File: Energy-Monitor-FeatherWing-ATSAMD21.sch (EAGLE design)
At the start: 32 parts

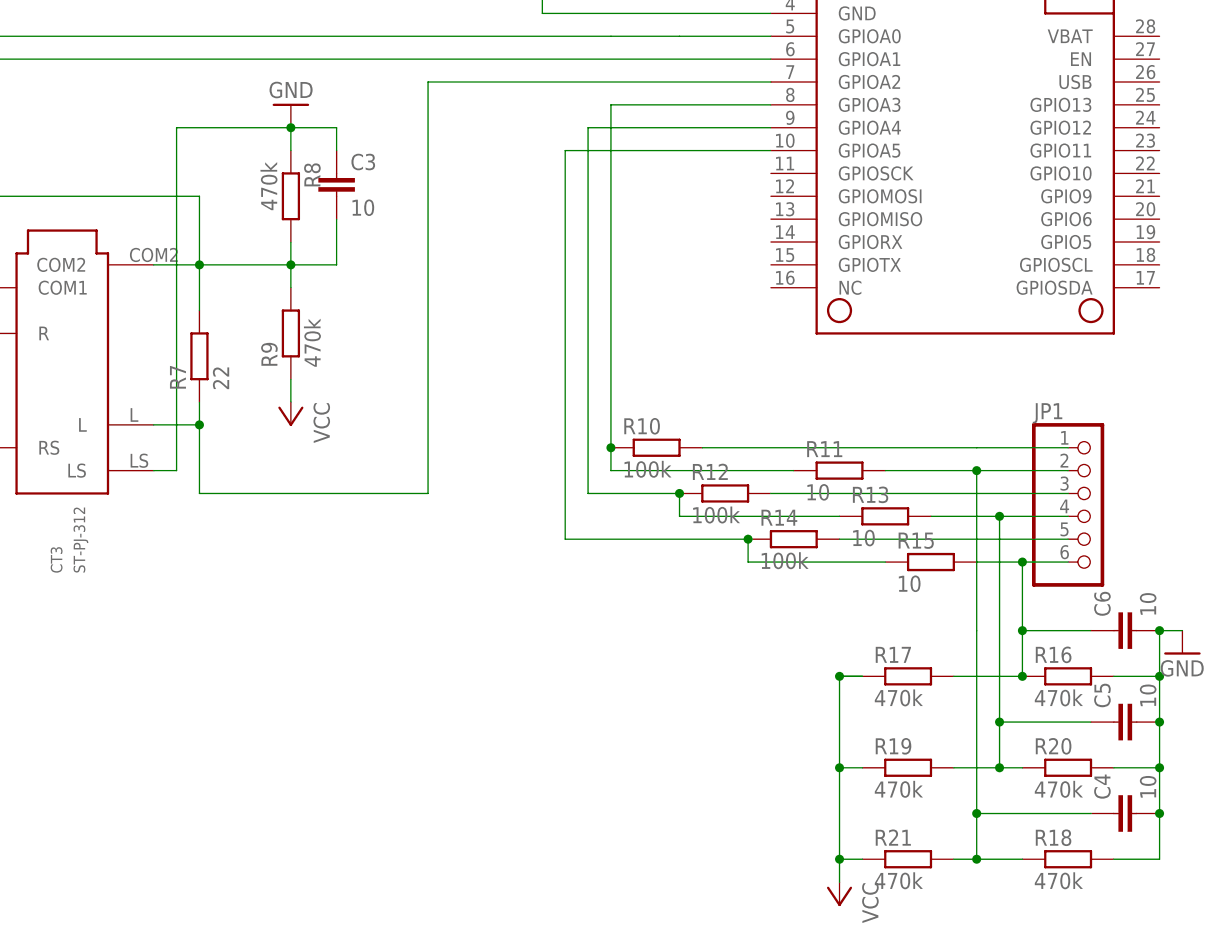
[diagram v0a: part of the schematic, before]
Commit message: Clean up layout and component names
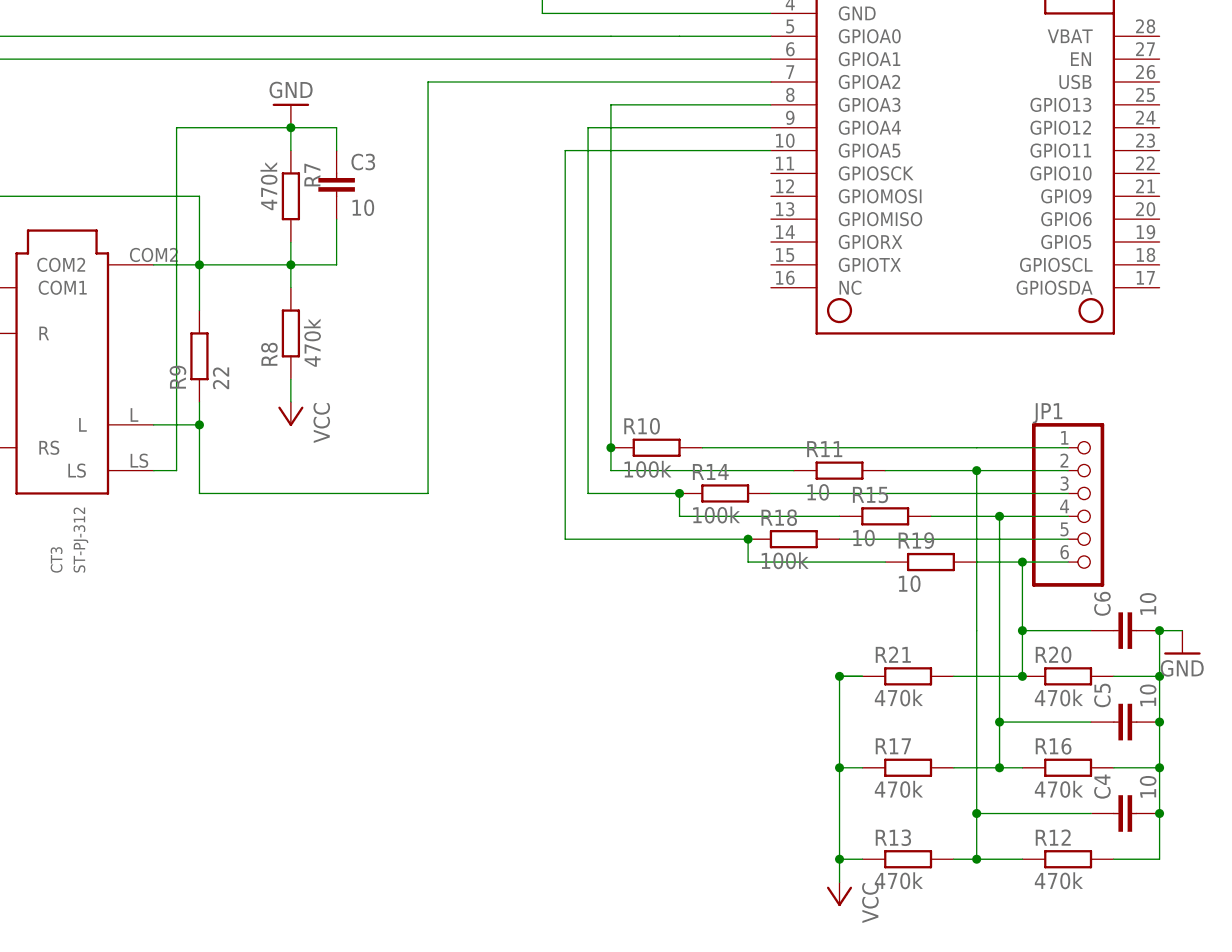
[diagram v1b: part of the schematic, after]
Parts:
- R12: value 100k -> 470k
- R13: value 10 -> 470k
- R18: value 470k -> 100k
- R19: value 470k -> 10
- R7: value 22 -> 470k
- R9: value 470k -> 22
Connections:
- net GND: now also R12.2, R7.1; no longer R18.2, R8.1
- net N$10: now also R18.2; no longer R14.2
- net N$11: now also R18.1, R19.1; no longer R14.1, R15.1
- net N$13: now also R15.2, R16.1, R17.2; no longer R13.2, R19.2, R20.1
- net N$3: now also R9.1; no longer R7.1
- net N$6: now also R19.2, R20.1, R21.2; no longer R15.2, R16.1, R17.2
- net N$7: now also R14.2; no longer R12.2
- net N$8: now also R14.1, R15.1; no longer R12.1, R13.1
- net N$9: now also R12.1, R13.2; no longer R18.1, R21.2
- net VCC: now also R13.1, R8.1; no longer R19.1, R9.1
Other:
- moved on the sheet: R12, R13, R14, R15, R16, R17, R18, R19, R20, R21, R7, R8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

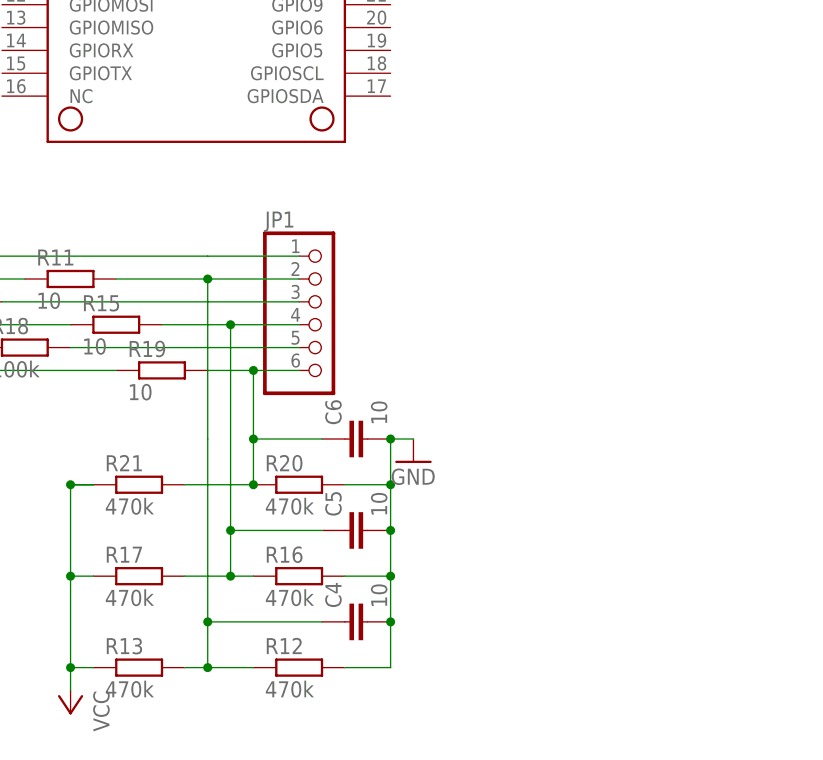
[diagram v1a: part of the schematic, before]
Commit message: Initial work on adding 3-phase bridge rectifier
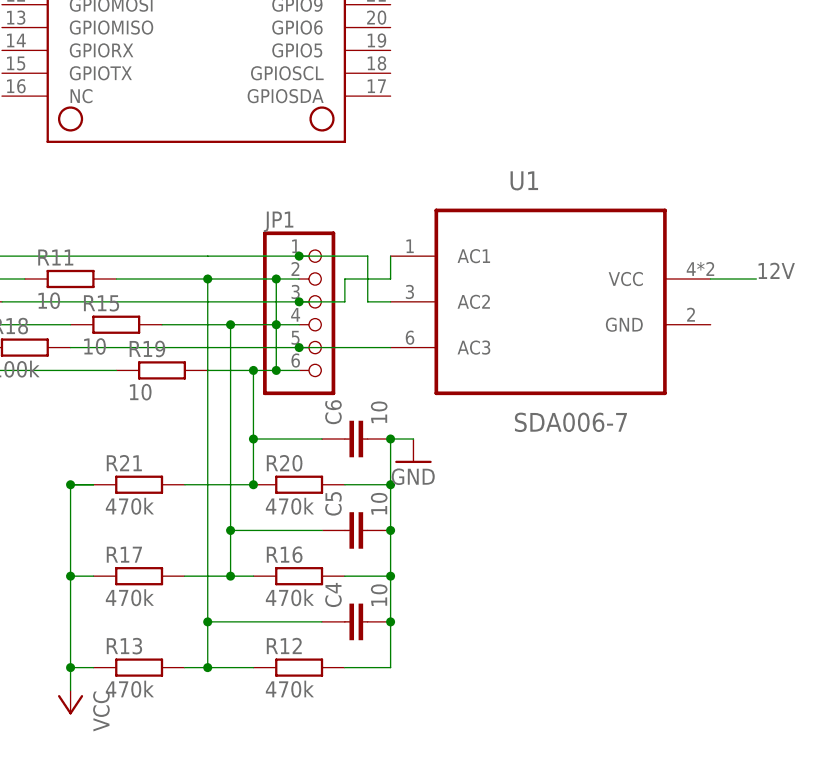
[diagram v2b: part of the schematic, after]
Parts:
- added U1: SDA006-7, Diodes_Inc_By_element14_Batch_1:SDA006-7
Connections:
- removed net N$13: C5.1, JP1.4, R15.2, R16.1, R17.2
- removed net N$6: C6.1, JP1.6, R19.2, R20.1, R21.2
- removed net N$9: C4.1, JP1.2, R11.2, R12.1, R13.2
- new net 12V: U1.VCC
- new net AC_GND: C4.1, C5.1, C6.1, JP1.2, JP1.4, JP1.6, R11.2, R12.1, R13.2, R15.2, R16.1, R17.2, R19.2, R20.1, R21.2
- net N$10: now also U1.AC3
- net N$4: now also U1.AC2
- net N$7: now also U1.AC1
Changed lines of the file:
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@@
 <?xml version="1.0" encoding="utf-8"?>
 <!DOCTYPE eagle SYSTEM "eagle.dtd">
-<eagle version="7.5.0">
+<eagle version="7.6.0">
 <drawing>
 <settings>
@@
 <part name="R16" library="resistor" deviceset="R-EU_" device="R0402" value="470k"/>
 <part name="R13" library="resistor" deviceset="R-EU_" device="R0402" value="470k"/>
+<part name="U1" library="Diodes_Inc_By_element14_Batch_1" deviceset="SDA006-7" device=""/>
 </parts>
 <sheets>
@@
 <instance part="R16" gate="G$1" x="190.5" y="-35.56"/>
 <instance part="R13" gate="G$1" x="172.72" y="-45.72"/>
+<instance part="U1" gate="G$1" x="218.44" y="-2.54"/>
 </instances>
 <busses>
@@
 <pinref part="R10" gate="G$1" pin="2"/>
 <wire x1="180.34" y1="0" x2="149.86" y2="0" width="0.1524" layer="91"/>
+<wire x1="190.5" y1="0" x2="198.12" y2="0" width="0.1524" layer="91"/>
+<wire x1="198.12" y1="0" x2="198.12" y2="-5.08" width="0.1524" layer="91"/>
+<junction x="190.5" y="0"/>
+<pinref part="U1" gate="G$1" pin="AC2"/>
+<wire x1="198.12" y1="-5.08" x2="200.66" y2="-5.08" width="0.1524" layer="91"/>
 </segment>
 </net>
@@
 <pinref part="R14" gate="G$1" pin="2"/>
 <wire x1="190.5" y1="-5.08" x2="157.48" y2="-5.08" width="0.1524" layer="91"/>
+<wire x1="190.5" y1="-5.08" x2="195.58" y2="-5.08" width="0.1524" layer="91"/>
+<junction x="190.5" y="-5.08"/>
+<wire x1="195.58" y1="-5.08" x2="195.58" y2="-2.54" width="0.1524" layer="91"/>
+<wire x1="195.58" y1="-2.54" x2="200.66" y2="-2.54" width="0.1524" layer="91"/>
+<pinref part="U1" gate="G$1" pin="AC1"/>
+<wire x1="200.66" y1="-2.54" x2="200.66" y2="0" width="0.1524" layer="91"/>
 </segment>
 </net>
@@
 </segment>
 </net>
-<net name="N$9" class="0">
+<net name="AC_GND" class="0">
 <segment>
 <pinref part="C4" gate="G$1" pin="1"/>
 <wire x1="193.04" y1="-40.64" x2="180.34" y2="-40.64" width="0.1524" layer="91"/>
-<wire x1="180.34" y1="-40.64" x2="180.34" y2="-20.32" width="0.1524" layer="91"/>
+<wire x1="180.34" y1="-40.64" x2="180.34" y2="-12.7" width="0.1524" layer="91"/>
 <pinref part="R11" gate="G$1" pin="2"/>
 <pinref part="JP1" gate="A" pin="2"/>
 <wire x1="170.18" y1="-2.54" x2="180.34" y2="-2.54" width="0.1524" layer="91"/>
-<wire x1="180.34" y1="-2.54" x2="190.5" y2="-2.54" width="0.1524" layer="91"/>
-<wire x1="180.34" y1="-20.32" x2="180.34" y2="-2.54" width="0.1524" layer="91"/>
+<wire x1="180.34" y1="-2.54" x2="187.96" y2="-2.54" width="0.1524" layer="91"/>
 <junction x="180.34" y="-2.54"/>
 <pinref part="R13" gate="G$1" pin="2"/>
 <pinref part="R12" gate="G$1" pin="1"/>
+<wire x1="187.96" y1="-2.54" x2="190.5" y2="-2.54" width="0.1524" layer="91"/>
+<wire x1="180.34" y1="-12.7" x2="180.34" y2="-2.54" width="0.1524" layer="91"/>
 <wire x1="185.42" y1="-45.72" x2="180.34" y2="-45.72" width="0.1524" layer="91"/>
 <wire x1="180.34" y1="-45.72" x2="177.8" y2="-45.72" width="0.1524" layer="91"/>
@@
 <junction x="180.34" y="-40.64"/>
 <junction x="180.34" y="-45.72"/>
-</segment>
-</net>
-<net name="N$10" class="0">
-<segment>
-<pinref part="R18" gate="G$1" pin="2"/>
-<pinref part="JP1" gate="A" pin="5"/>
-<wire x1="165.1" y1="-10.16" x2="182.88" y2="-10.16" width="0.1524" layer="91"/>
-<wire x1="182.88" y1="-10.16" x2="190.5" y2="-10.16" width="0.1524" layer="91"/>
-</segment>
-</net>
-<net name="N$11" class="0">
-<segment>
-<pinref part="R18" gate="G$1" pin="1"/>
-<wire x1="154.94" y1="-10.16" x2="154.94" y2="-12.7" width="0.1524" layer="91"/>
-<pinref part="R19" gate="G$1" pin="1"/>
-<wire x1="154.94" y1="-12.7" x2="170.18" y2="-12.7" width="0.1524" layer="91"/>
-<wire x1="154.94" y1="-10.16" x2="134.62" y2="-10.16" width="0.1524" layer="91"/>
-<junction x="154.94" y="-10.16"/>
-<wire x1="134.62" y1="-10.16" x2="134.62" y2="33.02" width="0.1524" layer="91"/>
-<pinref part="MS1" gate="G$1" pin="GPIOA5"/>
-<wire x1="134.62" y1="33.02" x2="157.48" y2="33.02" width="0.1524" layer="91"/>
-</segment>
-</net>
-<net name="N$13" class="0">
-<segment>
-<pinref part="C5" gate="G$1" pin="1"/>
-<wire x1="193.04" y1="-30.48" x2="182.88" y2="-30.48" width="0.1524" layer="91"/>
-<pinref part="JP1" gate="A" pin="4"/>
-<wire x1="180.34" y1="-7.62" x2="182.88" y2="-7.62" width="0.1524" layer="91"/>
-<pinref part="R15" gate="G$1" pin="2"/>
-<wire x1="182.88" y1="-7.62" x2="190.5" y2="-7.62" width="0.1524" layer="91"/>
-<wire x1="175.26" y1="-7.62" x2="180.34" y2="-7.62" width="0.1524" layer="91"/>
-<wire x1="182.88" y1="-30.48" x2="182.88" y2="-7.62" width="0.1524" layer="91"/>
-<junction x="182.88" y="-7.62"/>
-<wire x1="182.88" y1="-30.48" x2="182.88" y2="-35.56" width="0.1524" layer="91"/>
-<junction x="182.88" y="-30.48"/>
-<pinref part="R16" gate="G$1" pin="1"/>
-<wire x1="182.88" y1="-35.56" x2="185.42" y2="-35.56" width="0.1524" layer="91"/>
-<pinref part="R17" gate="G$1" pin="2"/>
-<wire x1="182.88" y1="-35.56" x2="177.8" y2="-35.56" width="0.1524" layer="91"/>
-<junction x="182.88" y="-35.56"/>
-</segment>
-</net>
-<net name="N$6" class="0">
-<segment>
 <pinref part="JP1" gate="A" pin="6"/>
-<wire x1="185.42" y1="-12.7" x2="190.5" y2="-12.7" width="0.1524" layer="91"/>
+<wire x1="185.42" y1="-12.7" x2="187.96" y2="-12.7" width="0.1524" layer="91"/>
 <pinref part="R19" gate="G$1" pin="2"/>
+<wire x1="187.96" y1="-12.7" x2="190.5" y2="-12.7" width="0.1524" layer="91"/>
 <wire x1="180.34" y1="-12.7" x2="185.42" y2="-12.7" width="0.1524" layer="91"/>
 <wire x1="185.42" y1="-12.7" x2="185.42" y2="-20.32" width="0.1524" layer="91"/>
@@
 <wire x1="177.8" y1="-25.4" x2="185.42" y2="-25.4" width="0.1524" layer="91"/>
 <junction x="185.42" y="-25.4"/>
-</segment>
-</net>
+<pinref part="R17" gate="G$1" pin="2"/>
+<pinref part="R16" gate="G$1" pin="1"/>
+<pinref part="JP1" gate="A" pin="4"/>
+<wire x1="182.88" y1="-7.62" x2="187.96" y2="-7.62" width="0.1524" layer="91"/>
+<pinref part="R15" gate="G$1" pin="2"/>
+<wire x1="187.96" y1="-7.62" x2="190.5" y2="-7.62" width="0.1524" layer="91"/>
+<wire x1="175.26" y1="-7.62" x2="182.88" y2="-7.62" width="0.1524" layer="91"/>
+<junction x="182.88" y="-7.62"/>
+<pinref part="C5" gate="G$1" pin="1"/>
+<wire x1="193.04" y1="-30.48" x2="182.88" y2="-30.48" width="0.1524" layer="91"/>
+<wire x1="182.88" y1="-30.48" x2="182.88" y2="-7.62" width="0.1524" layer="91"/>
+<junction x="182.88" y="-30.48"/>
+<wire x1="182.88" y1="-30.48" x2="182.88" y2="-35.56" width="0.1524" layer="91"/>
+<wire x1="182.88" y1="-35.56" x2="185.42" y2="-35.56" width="0.1524" layer="91"/>
+<junction x="182.88" y="-35.56"/>
+<wire x1="182.88" y1="-35.56" x2="177.8" y2="-35.56" width="0.1524" layer="91"/>
+<wire x1="187.96" y1="-2.54" x2="187.96" y2="-7.62" width="0.1524" layer="91"/>
+<junction x="187.96" y="-2.54"/>
+<junction x="187.96" y="-7.62"/>
+<wire x1="187.96" y1="-7.62" x2="187.96" y2="-12.7" width="0.1524" layer="91"/>
+<junction x="187.96" y="-12.7"/>
+</segment>
+</net>
+<net name="N$10" class="0">
+<segment>
+<pinref part="R18" gate="G$1" pin="2"/>
+<pinref part="JP1" gate="A" pin="5"/>
+<wire x1="165.1" y1="-10.16" x2="182.88" y2="-10.16" width="0.1524" layer="91"/>
+<wire x1="182.88" y1="-10.16" x2="190.5" y2="-10.16" width="0.1524" layer="91"/>
+<pinref part="U1" gate="G$1" pin="AC3"/>
+<wire x1="200.66" y1="-10.16" x2="190.5" y2="-10.16" width="0.1524" layer="91"/>
+<junction x="190.5" y="-10.16"/>
+</segment>
+</net>
+<net name="N$11" class="0">
+<segment>
+<pinref part="R18" gate="G$1" pin="1"/>
+<wire x1="154.94" y1="-10.16" x2="154.94" y2="-12.7" width="0.1524" layer="91"/>
+<pinref part="R19" gate="G$1" pin="1"/>
+<wire x1="154.94" y1="-12.7" x2="170.18" y2="-12.7" width="0.1524" layer="91"/>
+<wire x1="154.94" y1="-10.16" x2="134.62" y2="-10.16" width="0.1524" layer="91"/>
+<junction x="154.94" y="-10.16"/>
+<wire x1="134.62" y1="-10.16" x2="134.62" y2="33.02" width="0.1524" layer="91"/>
+<pinref part="MS1" gate="G$1" pin="GPIOA5"/>
+<wire x1="134.62" y1="33.02" x2="157.48" y2="33.02" width="0.1524" layer="91"/>
+</segment>
+</net>
+<net name="12V" class="0">
+<segment>
+<pinref part="U1" gate="G$1" pin="VCC"/>
+<wire x1="236.22" y1="-2.54" x2="241.3" y2="-2.54" width="0.1524" layer="91"/>
+<label x="241.3" y="-2.54" size="1.778" layer="95"/>
+</segment>
+</net>
